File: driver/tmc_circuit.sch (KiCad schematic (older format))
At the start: 3 parts, among them U2 TMC2208_SILENTSTEPSTICK

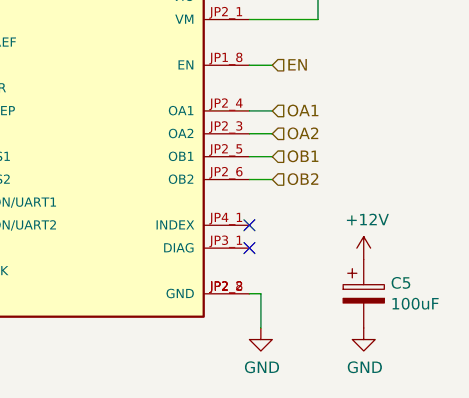
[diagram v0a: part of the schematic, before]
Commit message: Added connector project, mostly laid out driver.
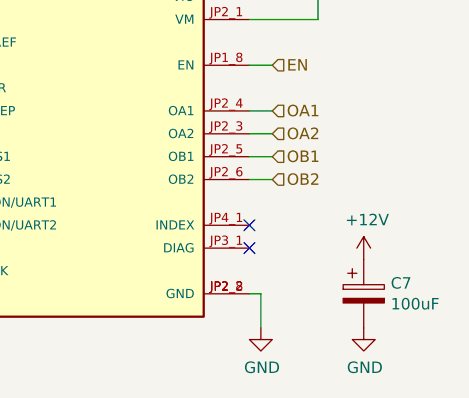
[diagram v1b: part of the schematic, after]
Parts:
- renumbered C4 to C6
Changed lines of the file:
@@
 P 7000 4000
 AR Path="/6024869C" Ref="C?"  Part="1"
-AR Path="/6023FC94/6024869C" Ref="C4"  Part="1"
-AR Path="/60256860/6024869C" Ref="C5"  Part="1"
-F 0 "C5" H 7118 4046 50  0000 L CNN
+AR Path="/6023FC94/6024869C" Ref="C6"  Part="1"
+AR Path="/60256860/6024869C" Ref="C7"  Part="1"
+F 0 "C7" H 7118 4046 50  0000 L CNN
 F 1 "100uF" H 7118 3955 50  0000 L CNN
 F 2 "Capacitor_SMD:CP_Elec_6.3x5.8" H 7038 3850 50  0001 C CNN
@@
 P 7000 3850
 AR Path="/602486A2" Ref="#PWR?"  Part="1"
-AR Path="/6023FC94/602486A2" Ref="#PWR019"  Part="1"
-AR Path="/60256860/602486A2" Ref="#PWR024"  Part="1"
-F 0 "#PWR024" H 7000 3700 50  0001 C CNN
+AR Path="/6023FC94/602486A2" Ref="#PWR0128"  Part="1"
+AR Path="/60256860/602486A2" Ref="#PWR0133"  Part="1"
+F 0 "#PWR0133" H 7000 3700 50  0001 C CNN
 F 1 "+12V" H 7015 4023 50  0000 C CNN
 F 2 "" H 7000 3850 50  0001 C CNN
@@
 P 7000 4150
 AR Path="/602486A8" Ref="#PWR?"  Part="1"
-AR Path="/6023FC94/602486A8" Ref="#PWR020"  Part="1"
-AR Path="/60256860/602486A8" Ref="#PWR025"  Part="1"
-F 0 "#PWR025" H 7000 3900 50  0001 C CNN
+AR Path="/6023FC94/602486A8" Ref="#PWR0129"  Part="1"
+AR Path="/60256860/602486A8" Ref="#PWR0134"  Part="1"
+F 0 "#PWR0134" H 7000 3900 50  0001 C CNN
 F 1 "GND" H 7005 3977 50  0000 C CNN
 F 2 "" H 7000 4150 50  0001 C CNN
@@
 P 6550 4150
 AR Path="/602486AE" Ref="#PWR?"  Part="1"
-AR Path="/6023FC94/602486AE" Ref="#PWR017"  Part="1"
-AR Path="/60256860/602486AE" Ref="#PWR022"  Part="1"
-F 0 "#PWR022" H 6550 3900 50  0001 C CNN
+AR Path="/6023FC94/602486AE" Ref="#PWR0130"  Part="1"
+AR Path="/60256860/602486AE" Ref="#PWR0135"  Part="1"
+F 0 "#PWR0135" H 6550 3900 50  0001 C CNN
 F 1 "GND" H 6555 3977 50  0000 C CNN
 F 2 "" H 6550 4150 50  0001 C CNN
@@
 P 6550 2650
 AR Path="/602486B5" Ref="#PWR?"  Part="1"
-AR Path="/6023FC94/602486B5" Ref="#PWR016"  Part="1"
-AR Path="/60256860/602486B5" Ref="#PWR021"  Part="1"
-F 0 "#PWR021" H 6550 2500 50  0001 C CNN
+AR Path="/6023FC94/602486B5" Ref="#PWR0131"  Part="1"
+AR Path="/60256860/602486B5" Ref="#PWR0136"  Part="1"
+F 0 "#PWR0136" H 6550 2500 50  0001 C CNN
 F 1 "+5V" H 6565 2823 50  0000 C CNN
 F 2 "" H 6550 2650 50  0001 C CNN
@@
 P 6800 2650
 AR Path="/602486BD" Ref="#PWR?"  Part="1"
-AR Path="/6023FC94/602486BD" Ref="#PWR018"  Part="1"
-AR Path="/60256860/602486BD" Ref="#PWR023"  Part="1"
-F 0 "#PWR023" H 6800 2500 50  0001 C CNN
+AR Path="/6023FC94/602486BD" Ref="#PWR0132"  Part="1"
+AR Path="/60256860/602486BD" Ref="#PWR0137"  Part="1"
+F 0 "#PWR0137" H 6800 2500 50  0001 C CNN
 F 1 "+12V" H 6815 2823 50  0000 C CNN
 F 2 "" H 6800 2650 50  0001 C CNN

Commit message: Added BOM, re-organized things a bit
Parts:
- U2: Digi-Key Part Number (none) -> 1460-1201-ND; MANUFACTURER Trinamic -> (none); MAXIMUM_PACKAGE_HEIGHT N/A -> (none); PARTREV v11 -> (none); STANDARD Manufacturer Recommendations -> (none)
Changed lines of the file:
@@
 encoding utf-8
 Sheet 3 3
-Title ""
-Date ""
-Rev ""
-Comp ""
+Title "Silent Dripper Driver"
+Date "2021-02-09"
+Rev "1.0.0"
+Comp "www.esologic.com"
 Comment1 ""
 Comment2 ""
 Comment3 ""
-Comment4 ""
+Comment4 "For support, email dev@esologic.com"
 $EndDescr
 $Comp
@@
 F 1 "TMC2208_SILENTSTEPSTICK" H 5800 4076 50  0000 C CNN
 F 2 "TMC2208_SILENTSTEPSTICK:MODULE_TMC2208_SILENTSTEPSTICK" H 5800 3300 50  0001 L BNN
-F 3 "" H 5800 3300 50  0001 L BNN
-F 4 "N/A" H 5800 3300 50  0001 L BNN "MAXIMUM_PACKAGE_HEIGHT"
-F 5 "v11" H 5800 3300 50  0001 L BNN "PARTREV"
-F 6 "Trinamic" H 5800 3300 50  0001 L BNN "MANUFACTURER"
-F 7 "Manufacturer Recommendations" H 5800 3300 50  0001 L BNN "STANDARD"
+F 3 "https://www.trinamic.com/fileadmin/assets/Products/ICs_Documents/TMC220x_TMC2224_datasheet_Rev1.09.pdf" H 5800 3300 50  0001 L BNN
+F 4 "1460-1201-ND" H 5800 3300 50  0001 C CNN "Digi-Key Part Number"
 	1    5800 3300
 	1    0    0    -1

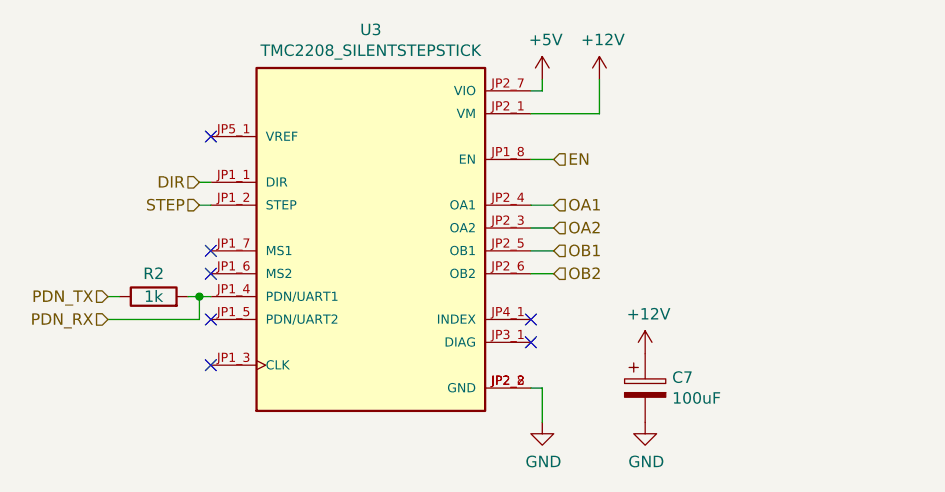
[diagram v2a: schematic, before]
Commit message: Routed both boards, happy. Hopefully the traces are thick enough, used an only calculator given max rated draw of the TMCs
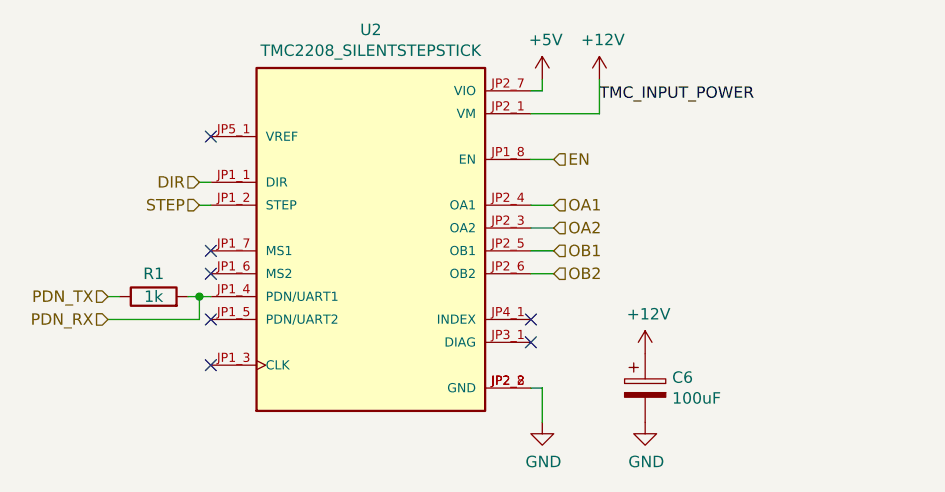
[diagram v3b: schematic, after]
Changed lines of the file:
@@
 $Descr A4 11693 8268
 encoding utf-8
-Sheet 3 3
+Sheet 2 3
 Title "Silent Dripper Driver"
 Date "2021-02-09"
@@
 AR Path="/6023FC94/6024869C" Ref="C6"  Part="1"
 AR Path="/60256860/6024869C" Ref="C7"  Part="1"
-F 0 "C7" H 7118 4046 50  0000 L CNN
+F 0 "C6" H 7118 4046 50  0000 L CNN
 F 1 "100uF" H 7118 3955 50  0000 L CNN
 F 2 "Capacitor_SMD:CP_Elec_6.3x5.8" H 7038 3850 50  0001 C CNN
@@
 AR Path="/6023FC94/602486A2" Ref="#PWR0128"  Part="1"
 AR Path="/60256860/602486A2" Ref="#PWR0133"  Part="1"
-F 0 "#PWR0133" H 7000 3700 50  0001 C CNN
+F 0 "#PWR0128" H 7000 3700 50  0001 C CNN
 F 1 "+12V" H 7015 4023 50  0000 C CNN
 F 2 "" H 7000 3850 50  0001 C CNN
@@
 AR Path="/6023FC94/602486A8" Ref="#PWR0129"  Part="1"
 AR Path="/60256860/602486A8" Ref="#PWR0134"  Part="1"
-F 0 "#PWR0134" H 7000 3900 50  0001 C CNN
+F 0 "#PWR0129" H 7000 3900 50  0001 C CNN
 F 1 "GND" H 7005 3977 50  0000 C CNN
 F 2 "" H 7000 4150 50  0001 C CNN
@@
 AR Path="/6023FC94/602486AE" Ref="#PWR0130"  Part="1"
 AR Path="/60256860/602486AE" Ref="#PWR0135"  Part="1"
-F 0 "#PWR0135" H 6550 3900 50  0001 C CNN
+F 0 "#PWR0130" H 6550 3900 50  0001 C CNN
 F 1 "GND" H 6555 3977 50  0000 C CNN
 F 2 "" H 6550 4150 50  0001 C CNN
@@
 AR Path="/6023FC94/602486B5" Ref="#PWR0131"  Part="1"
 AR Path="/60256860/602486B5" Ref="#PWR0136"  Part="1"
-F 0 "#PWR0136" H 6550 2500 50  0001 C CNN
+F 0 "#PWR0131" H 6550 2500 50  0001 C CNN
 F 1 "+5V" H 6565 2823 50  0000 C CNN
 F 2 "" H 6550 2650 50  0001 C CNN
@@
 AR Path="/6023FC94/602486BD" Ref="#PWR0132"  Part="1"
 AR Path="/60256860/602486BD" Ref="#PWR0137"  Part="1"
-F 0 "#PWR0137" H 6800 2500 50  0001 C CNN
+F 0 "#PWR0132" H 6800 2500 50  0001 C CNN
 F 1 "+12V" H 6815 2823 50  0000 C CNN
 F 2 "" H 6800 2650 50  0001 C CNN
@@
 AR Path="/6023FC94/602486C9" Ref="U2"  Part="1"
 AR Path="/60256860/602486C9" Ref="U3"  Part="1"
-F 0 "U3" H 5800 4167 50  0000 C CNN
+F 0 "U2" H 5800 4167 50  0000 C CNN
 F 1 "TMC2208_SILENTSTEPSTICK" H 5800 4076 50  0000 C CNN
 F 2 "TMC2208_SILENTSTEPSTICK:MODULE_TMC2208_SILENTSTEPSTICK" H 5800 3300 50  0001 L BNN
@@
 AR Path="/6023FC94/602486D9" Ref="R1"  Part="1"
 AR Path="/60256860/602486D9" Ref="R2"  Part="1"
-F 0 "R2" V 4950 3600 50  0000 C CNN
+F 0 "R1" V 4950 3600 50  0000 C CNN
 F 1 "1k" V 4850 3600 50  0000 C CNN
 F 2 "Capacitor_SMD:C_0805_2012Metric_Pad1.18x1.45mm_HandSolder" V 4780 3600 50  0001 C CNN
@@
 Wire Wire Line
 	6500 3500 6600 3500
+Text Label 6800 2750 0    50   ~ 0
+TMC_INPUT_POWER
 $EndSCHEMATC

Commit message: Fit test passed, panelized boards. Ready to order soon
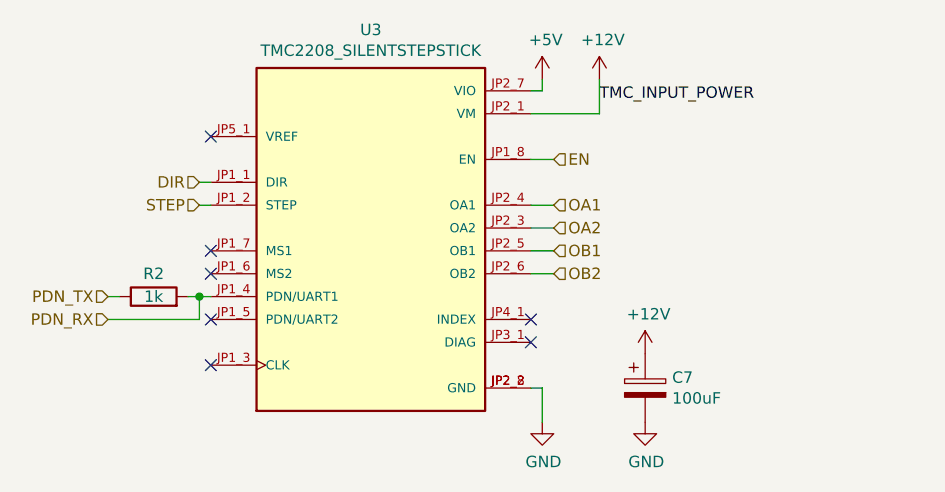
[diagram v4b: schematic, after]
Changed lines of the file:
@@
 $Descr A4 11693 8268
 encoding utf-8
-Sheet 2 3
+Sheet 3 3
 Title "Silent Dripper Driver"
 Date "2021-02-09"
@@
 AR Path="/6023FC94/6024869C" Ref="C6"  Part="1"
 AR Path="/60256860/6024869C" Ref="C7"  Part="1"
-F 0 "C6" H 7118 4046 50  0000 L CNN
+F 0 "C7" H 7118 4046 50  0000 L CNN
 F 1 "100uF" H 7118 3955 50  0000 L CNN
 F 2 "Capacitor_SMD:CP_Elec_6.3x5.8" H 7038 3850 50  0001 C CNN
@@
 AR Path="/6023FC94/602486A2" Ref="#PWR0128"  Part="1"
 AR Path="/60256860/602486A2" Ref="#PWR0133"  Part="1"
-F 0 "#PWR0128" H 7000 3700 50  0001 C CNN
+F 0 "#PWR0133" H 7000 3700 50  0001 C CNN
 F 1 "+12V" H 7015 4023 50  0000 C CNN
 F 2 "" H 7000 3850 50  0001 C CNN
@@
 AR Path="/6023FC94/602486A8" Ref="#PWR0129"  Part="1"
 AR Path="/60256860/602486A8" Ref="#PWR0134"  Part="1"
-F 0 "#PWR0129" H 7000 3900 50  0001 C CNN
+F 0 "#PWR0134" H 7000 3900 50  0001 C CNN
 F 1 "GND" H 7005 3977 50  0000 C CNN
 F 2 "" H 7000 4150 50  0001 C CNN
@@
 AR Path="/6023FC94/602486AE" Ref="#PWR0130"  Part="1"
 AR Path="/60256860/602486AE" Ref="#PWR0135"  Part="1"
-F 0 "#PWR0130" H 6550 3900 50  0001 C CNN
+F 0 "#PWR0135" H 6550 3900 50  0001 C CNN
 F 1 "GND" H 6555 3977 50  0000 C CNN
 F 2 "" H 6550 4150 50  0001 C CNN
@@
 AR Path="/6023FC94/602486B5" Ref="#PWR0131"  Part="1"
 AR Path="/60256860/602486B5" Ref="#PWR0136"  Part="1"
-F 0 "#PWR0131" H 6550 2500 50  0001 C CNN
+F 0 "#PWR0136" H 6550 2500 50  0001 C CNN
 F 1 "+5V" H 6565 2823 50  0000 C CNN
 F 2 "" H 6550 2650 50  0001 C CNN
@@
 AR Path="/6023FC94/602486BD" Ref="#PWR0132"  Part="1"
 AR Path="/60256860/602486BD" Ref="#PWR0137"  Part="1"
-F 0 "#PWR0132" H 6800 2500 50  0001 C CNN
+F 0 "#PWR0137" H 6800 2500 50  0001 C CNN
 F 1 "+12V" H 6815 2823 50  0000 C CNN
 F 2 "" H 6800 2650 50  0001 C CNN
@@
 AR Path="/6023FC94/602486C9" Ref="U2"  Part="1"
 AR Path="/60256860/602486C9" Ref="U3"  Part="1"
-F 0 "U2" H 5800 4167 50  0000 C CNN
+F 0 "U3" H 5800 4167 50  0000 C CNN
 F 1 "TMC2208_SILENTSTEPSTICK" H 5800 4076 50  0000 C CNN
 F 2 "TMC2208_SILENTSTEPSTICK:MODULE_TMC2208_SILENTSTEPSTICK" H 5800 3300 50  0001 L BNN
@@
 AR Path="/6023FC94/602486D9" Ref="R1"  Part="1"
 AR Path="/60256860/602486D9" Ref="R2"  Part="1"
-F 0 "R1" V 4950 3600 50  0000 C CNN
+F 0 "R2" V 4950 3600 50  0000 C CNN
 F 1 "1k" V 4850 3600 50  0000 C CNN
 F 2 "Capacitor_SMD:C_0805_2012Metric_Pad1.18x1.45mm_HandSolder" V 4780 3600 50  0001 C CNN

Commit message: Design is finished, ordering boards
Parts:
- added C9: 47uF/6.3V, Capacitor_SMD:CP_Elec_5x5.7, symbol Device:CP
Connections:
- net +5V: now also C9.1
- net GND: now also C9.2
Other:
- moved on the sheet: C7
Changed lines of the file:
@@
 L Device:CP C?
 U 1 1 6024869C
-P 7000 4000
+P 7150 3100
 AR Path="/6024869C" Ref="C?"  Part="1"
 AR Path="/6023FC94/6024869C" Ref="C6"  Part="1"
 AR Path="/60256860/6024869C" Ref="C7"  Part="1"
-F 0 "C7" H 7118 4046 50  0000 L CNN
-F 1 "100uF" H 7118 3955 50  0000 L CNN
-F 2 "Capacitor_SMD:CP_Elec_6.3x5.8" H 7038 3850 50  0001 C CNN
-F 3 "http://nichicon-us.com/english/products/pdfs/e-uwj.pdf" H 7000 4000 50  0001 C CNN
-F 4 "493-9777-1-ND" H 7000 4000 50  0001 C CNN "Digi-Key Part Number"
-	1    7000 4000
-	1    0    0    -1
-$EndComp
-$Comp
-L power:+12V #PWR?
-U 1 1 602486A2
-P 7000 3850
-AR Path="/602486A2" Ref="#PWR?"  Part="1"
-AR Path="/6023FC94/602486A2" Ref="#PWR0128"  Part="1"
-AR Path="/60256860/602486A2" Ref="#PWR0133"  Part="1"
-F 0 "#PWR0133" H 7000 3700 50  0001 C CNN
-F 1 "+12V" H 7015 4023 50  0000 C CNN
-F 2 "" H 7000 3850 50  0001 C CNN
-F 3 "" H 7000 3850 50  0001 C CNN
-	1    7000 3850
+F 0 "C7" H 7268 3146 50  0000 L CNN
+F 1 "100uF" H 7268 3055 50  0000 L CNN
+F 2 "Capacitor_SMD:CP_Elec_6.3x5.8" H 7188 2950 50  0001 C CNN
+F 3 "http://nichicon-us.com/english/products/pdfs/e-uwj.pdf" H 7150 3100 50  0001 C CNN
+F 4 "493-9777-1-ND" H 7150 3100 50  0001 C CNN "Digi-Key Part Number"
+	1    7150 3100
 	1    0    0    -1
 $EndComp
@@
 L power:GND #PWR?
 U 1 1 602486A8
-P 7000 4150
+P 7150 4150
 AR Path="/602486A8" Ref="#PWR?"  Part="1"
 AR Path="/6023FC94/602486A8" Ref="#PWR0129"  Part="1"
 AR Path="/60256860/602486A8" Ref="#PWR0134"  Part="1"
-F 0 "#PWR0134" H 7000 3900 50  0001 C CNN
-F 1 "GND" H 7005 3977 50  0000 C CNN
-F 2 "" H 7000 4150 50  0001 C CNN
-F 3 "" H 7000 4150 50  0001 C CNN
-	1    7000 4150
+F 0 "#PWR0134" H 7150 3900 50  0001 C CNN
+F 1 "GND" H 7155 3977 50  0000 C CNN
+F 2 "" H 7150 4150 50  0001 C CNN
+F 3 "" H 7150 4150 50  0001 C CNN
+	1    7150 4150
 	1    0    0    -1
 $EndComp
@@
 L power:+5V #PWR?
 U 1 1 602486B5
-P 6550 2650
+P 7650 2650
 AR Path="/602486B5" Ref="#PWR?"  Part="1"
 AR Path="/6023FC94/602486B5" Ref="#PWR0131"  Part="1"
 AR Path="/60256860/602486B5" Ref="#PWR0136"  Part="1"
-F 0 "#PWR0136" H 6550 2500 50  0001 C CNN
-F 1 "+5V" H 6565 2823 50  0000 C CNN
-F 2 "" H 6550 2650 50  0001 C CNN
-F 3 "" H 6550 2650 50  0001 C CNN
-	1    6550 2650
-	1    0    0    -1
-$EndComp
-Wire Wire Line
-	6500 2700 6550 2700
-Wire Wire Line
-	6550 2700 6550 2650
+F 0 "#PWR0136" H 7650 2500 50  0001 C CNN
+F 1 "+5V" H 7665 2823 50  0000 C CNN
+F 2 "" H 7650 2650 50  0001 C CNN
+F 3 "" H 7650 2650 50  0001 C CNN
+	1    7650 2650
+	1    0    0    -1
+$EndComp
 $Comp
 L power:+12V #PWR?
 U 1 1 602486BD
-P 6800 2650
+P 7150 2650
 AR Path="/602486BD" Ref="#PWR?"  Part="1"
 AR Path="/6023FC94/602486BD" Ref="#PWR0132"  Part="1"
 AR Path="/60256860/602486BD" Ref="#PWR0137"  Part="1"
-F 0 "#PWR0137" H 6800 2500 50  0001 C CNN
-F 1 "+12V" H 6815 2823 50  0000 C CNN
-F 2 "" H 6800 2650 50  0001 C CNN
-F 3 "" H 6800 2650 50  0001 C CNN
-	1    6800 2650
-	1    0    0    -1
-$EndComp
-Wire Wire Line
-	6500 2800 6800 2800
-Wire Wire Line
-	6800 2800 6800 2650
+F 0 "#PWR0137" H 7150 2500 50  0001 C CNN
+F 1 "+12V" H 7165 2823 50  0000 C CNN
+F 2 "" H 7150 2650 50  0001 C CNN
+F 3 "" H 7150 2650 50  0001 C CNN
+	1    7150 2650
+	1    0    0    -1
+$EndComp
 $Comp
 L TMC2208_SILENTSTEPSTICK:TMC2208_SILENTSTEPSTICK U?
@@
 Wire Wire Line
 	6500 3500 6600 3500
-Text Label 6800 2750 0    50   ~ 0
-TMC_INPUT_POWER
+$Comp
+L Device:CP C?
+U 1 1 602C132B
+P 7650 3100
+AR Path="/602C132B" Ref="C?"  Part="1"
+AR Path="/6023FC94/602C132B" Ref="C9"  Part="1"
+AR Path="/60256860/602C132B" Ref="C10"  Part="1"
+F 0 "C10" H 7768 3146 50  0000 L CNN
+F 1 "47uF/6.3V" H 7768 3055 50  0000 L CNN
+F 2 "Capacitor_SMD:CP_Elec_5x5.7" H 7688 2950 50  0001 C CNN
+F 3 "http://nichicon-us.com/english/products/pdfs/e-uwj.pdf" H 7650 3100 50  0001 C CNN
+F 4 "493-9781-6-ND" H 7650 3100 50  0001 C CNN "Digi-Key Part Number"
+	1    7650 3100
+	1    0    0    -1
+$EndComp
+Wire Wire Line
+	7150 2800 7150 2650
+Wire Wire Line
+	6500 2800 7150 2800
+Wire Wire Line
+	7650 2700 7650 2650
+Wire Wire Line
+	6500 2700 7650 2700
+Wire Wire Line
+	7650 2700 7650 2950
+Connection ~ 7650 2700
+Wire Wire Line
+	7150 2950 7150 2800
+Connection ~ 7150 2800
+Wire Wire Line
+	7150 4150 7150 3250
+$Comp
+L power:GND #PWR?
+U 1 1 602CB31C
+P 7650 4150
+AR Path="/602CB31C" Ref="#PWR?"  Part="1"
+AR Path="/6023FC94/602CB31C" Ref="#PWR0133"  Part="1"
+AR Path="/60256860/602CB31C" Ref="#PWR0138"  Part="1"
+F 0 "#PWR0138" H 7650 3900 50  0001 C CNN
+F 1 "GND" H 7655 3977 50  0000 C CNN
+F 2 "" H 7650 4150 50  0001 C CNN
+F 3 "" H 7650 4150 50  0001 C CNN
+	1    7650 4150
+	1    0    0    -1
+$EndComp
+Wire Wire Line
+	7650 4150 7650 3250
 $EndSCHEMATC
